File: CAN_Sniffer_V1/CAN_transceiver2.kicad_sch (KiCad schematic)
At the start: 5 parts, among them J2 Conn_01x02, U2 MCP2562

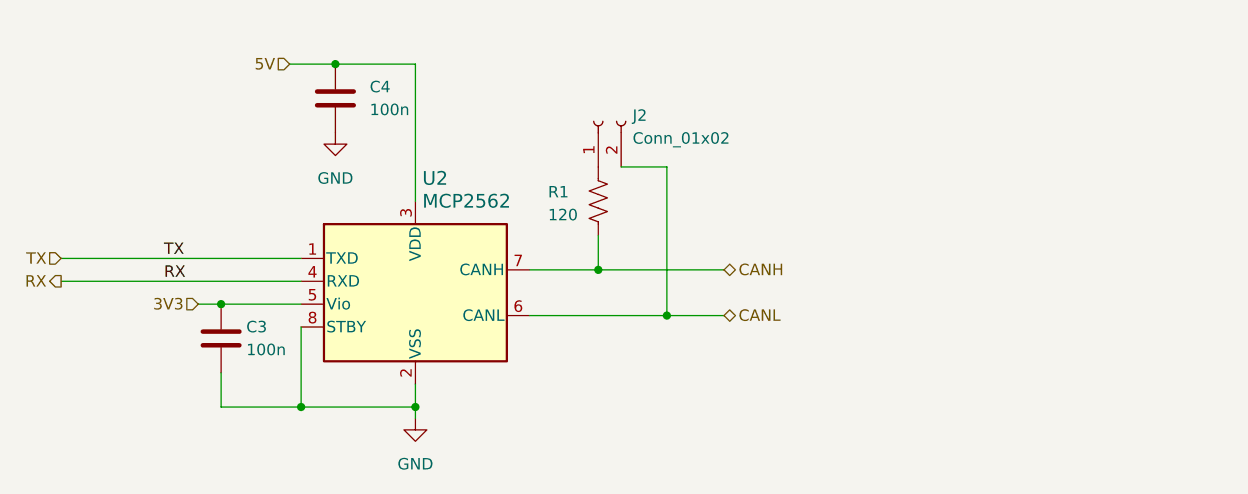
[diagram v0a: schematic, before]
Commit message: changed power schematics and STM32, added MicroSD card connector and LCD display
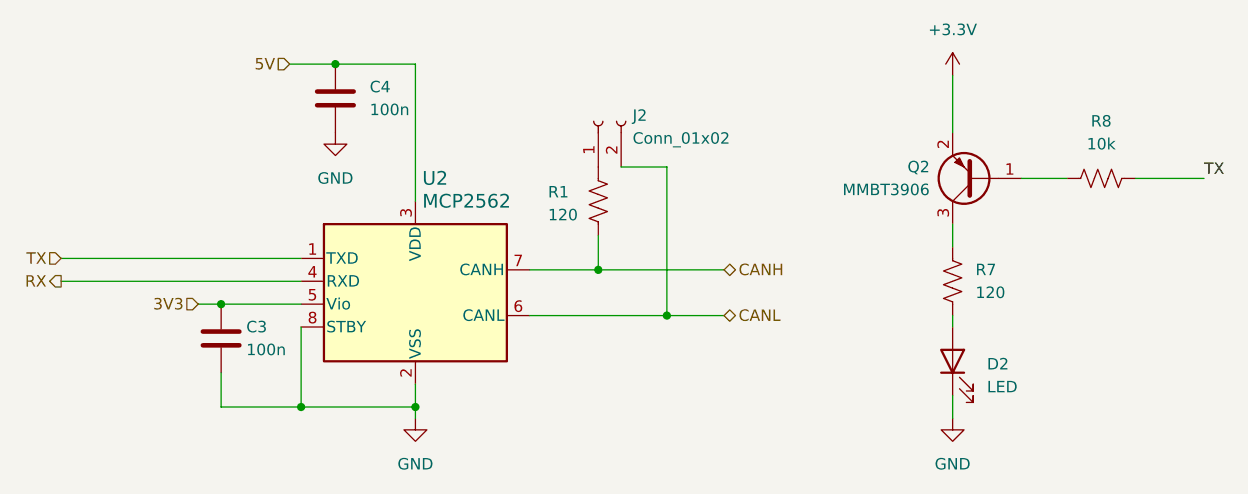
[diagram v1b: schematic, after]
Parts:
- added D2: LED, LED_SMD:LED_0805_2012Metric_Pad1.15x1.40mm_HandSolder, symbol Device:LED
- added Q2: MMBT3906, Package_TO_SOT_SMD:SOT-23, symbol Transistor_BJT:MMBT3906
- added R7: 120, Resistor_SMD:R_0805_2012Metric_Pad1.20x1.40mm_HandSolder, symbol Device:R_US
- added R8: 10k, Resistor_SMD:R_0805_2012Metric_Pad1.20x1.40mm_HandSolder, symbol Device:R_US
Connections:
- net GND: now also D2.1 (K)
- net TX: now also R8.2
- new net: Q2.1 (B), R8.1
- new net: Q2.3 (C), R7.1
- new net: D2.2 (A), R7.2
- new net +3.3V: Q2.2 (E)
